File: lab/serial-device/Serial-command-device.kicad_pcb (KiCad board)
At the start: 2 copper layers, 78 x 64 mm, 4 parts, among them U1 atmega168p

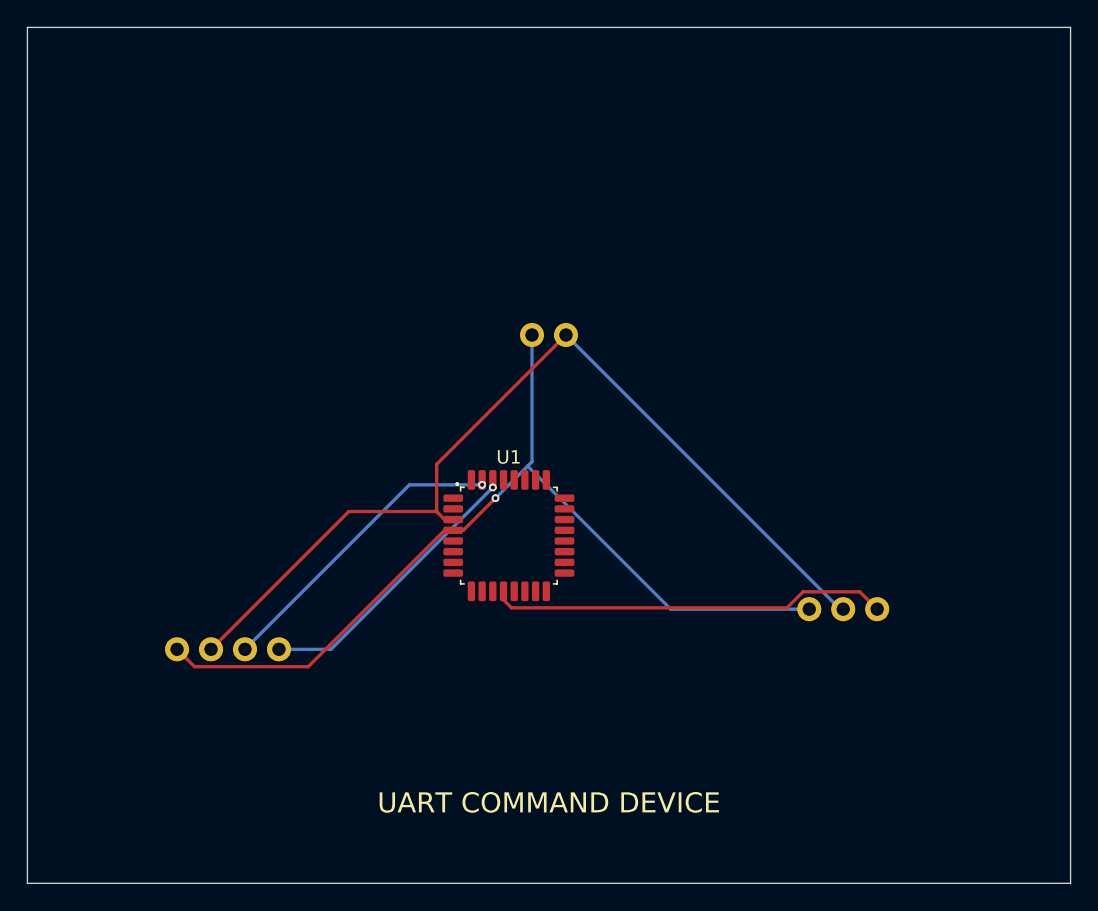
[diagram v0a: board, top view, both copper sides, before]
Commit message: lab: every board is a real board: an Arduino Nano and registry parts, routed, ready to order
The lab boards ran on simulation-only envelopes (labMcu, labDisplay, a battery). Now each is
an Arduino Nano on two sockets on the back (flashed over its USB, the image the app builds),
its lights LEDs through 1 kΩ, its knobs PTV09A pots, its display the MAX7219 eight-digit
module, its sensors an SHT31 and an SCD40 with their datasheets' support circuits, the FTDI
header for the serial console; the servo boards take 5 V on a screw terminal with a bulk
capacitor. All ten check complete with no errors or warnings, their firmware unchanged
(serial-device now on the 328P), and run in the lab without a fault (3 s each, dev host).

The registry: every interactive board must be ready to order and flash (publish.mjs refuses
one that is not; status simulation-only removed).

Claude-Session: https://claude.ai/code/session_01ATmMmxyrWxFwR3nTdXUrcx
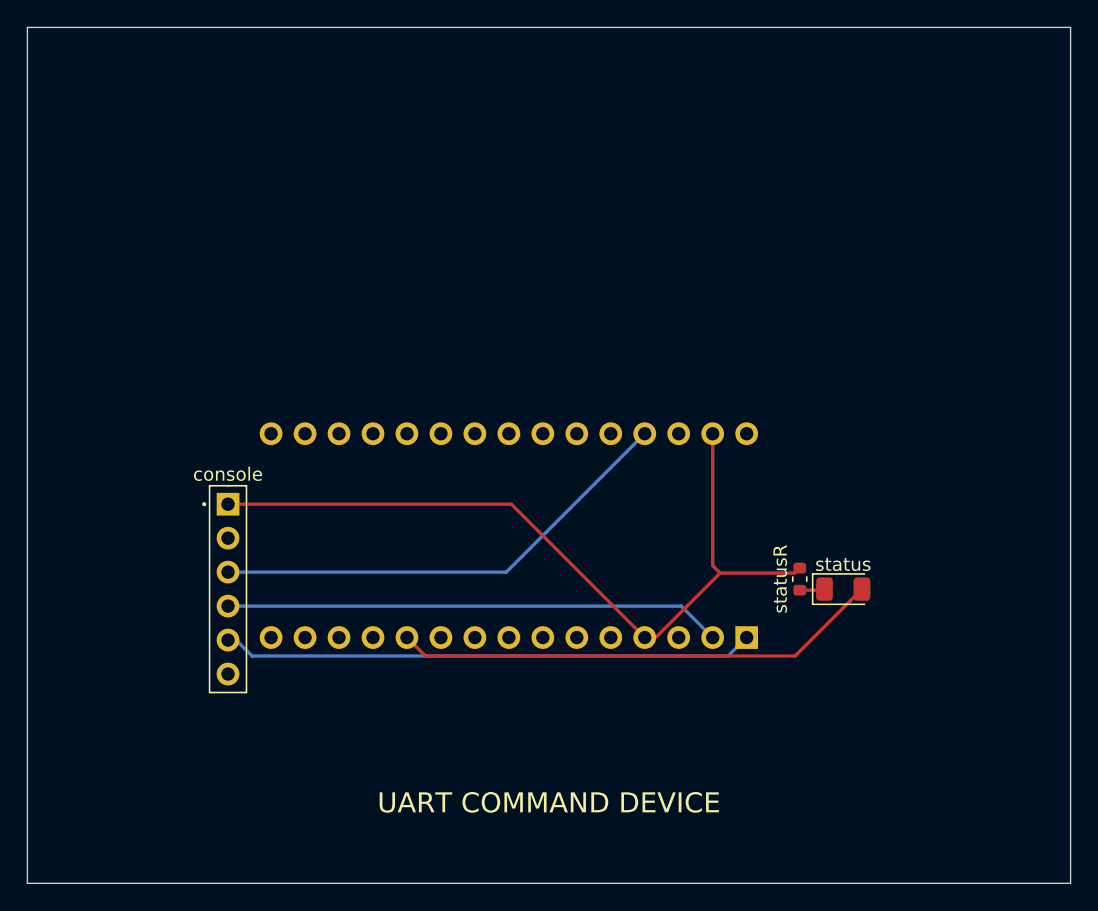
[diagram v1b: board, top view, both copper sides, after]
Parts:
- removed battery: battery, Regulated battery module
- removed the console at (115.0, 178.0)
- removed the status at (161.0, 178.0)
- added console: , PinHeader_1x06_P2.54mm_Vertical, F.Cu at (115.0, 178.0)
- added status: green, LED_1206_3216Metric, F.Cu at (161.0, 178.0)
- added statusR: 1kohm, R_0603_1608Metric, F.Cu at (157.8, 177.2)
- U1: value atmega168p -> A000005; footprint TQFP-32_7x7mm_P0.8mm -> Arduino_Nano_Socket_2x15_P2.54mm_W15.24mm; moved to B.Cu
- turned U1 to 90 degrees
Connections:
- U1 pad 1: (no net) -> TX
- U1 pad 11: (no net) -> LIGHT
- U1 pad 12: LIGHT -> (no net)
- U1 pad 2: (no net) -> RX
- U1 pad 27: (no net) -> V5
- U1 pad 29: (no net) -> GND
- U1 pad 3: GND -> (no net)
- U1 pad 30: RX -> (no net)
- U1 pad 4: V5 -> GND
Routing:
- net V5: track 68.4 -> 35.4 mm, vias 1 -> 0
- net TX: track 22.8 -> 39.8 mm, vias 1 -> 0
- net RX: track 21.0 -> 37.2 mm, vias 1 -> 0
- net GND: track 69.0 -> 58.3 mm
- net LIGHT: track 29.9 -> 36.7 mm
- net LIGHT_K: track 0.00 -> 2.09 mm

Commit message: Boards pass check and KiCad 10's DRC again: holes in courtyards, the USB net rename
pcbkit's check now has KiCad 10's pth/npth_inside_courtyard (pcbkit be5b6955), and 13 boards
failed it. KiCad's own DRC (kicad-cli 10) reports the same holes on every one of them.

- Parts that really stand above the holes under them (a screen or a Nano on its sockets, the
  Delta-S02's КМ-6 capacitors flat under its chips, as the factory placed them): a courtyard rule
  for the pair, written to each board's .kicad_dru, so KiCad's DRC agrees.
- Real collisions moved: servo-controller's dial 3 mm up (the Nano's socket pins came out under
  it), c3-pocket's fourth M3 hole from under a cell holder to the top edge's middle, s3-rgb's
  D-pad 2 mm up (a holder's peg came through under the down key).
- v003-emu, c3-pocket, rp2040-tft, rp2350-psram, s3-rgb, teensy41: re-routed for the standard USB
  block's renamed net (usb/raw is usb/vbusIn since pcbkit 2088839e): their tracks still carried
  the old name and shorted the fuse and connector pads.
- p4-touch-7: its board file still had a courtyard for the panel the design gives none (KiCad
  reported 114 courtyard errors); written again.

Measured on the dev host: all 44 registry boards `pcbkit check` complete with 0 errors, and
kicad-cli pcb drc 0 errors on every board.

Claude-Session: https://claude.ai/code/session_018URVYF1YPgyrMNetY9yT1T
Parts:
- console: value (none) -> PinHeader_1x06_P2.54mm_Vertical
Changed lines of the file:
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@@
   (footprint "Arduino_Nano_Socket_2x15_P2.54mm_W15.24mm" (layer "B.Cu") (at 136 174 90)
     (descr "Arduino Nano on two 1x15 female headers 15.24 mm apart, its USB end at +Y (Arduino's drawing): pins 1-15 the right row from the bottom (D1/TX … D12), 16-30 the left row from the top (D13 … VIN)")
+    (tags "THT module pin socket female header")
     (property "Reference" "U1" (at 0 -24.05 90) (layer "B.SilkS") (effects (font (size 1 1) (thickness 0.15)) (justify mirror)))
     (property "Value" "A000005" (at 0 0 0) (layer "B.Fab") (hide yes) (effects (font (size 1 1))))
@@
     (property "Status" "checked" (at 0 0 0) (layer "B.Fab") (hide yes) (effects (font (size 1 1))))
     (property "pcbkit" "U1" (at 0 0 0) (layer "B.Fab") (hide yes) (effects (font (size 1 1))))
-    (duplicate_pad_numbers_are_jumpers no)
     (fp_rect (start 9.25 21.85) (end -9.25 -23.35) (stroke (width 0.05) (type solid)) (layer "B.CrtYd"))
     (fp_line (start 0 -23.21) (end 9.11 -23.21) (stroke (width 0.12) (type solid)) (layer "B.SilkS"))
@@
   (footprint "PinHeader_1x06_P2.54mm_Vertical" (layer "F.Cu") (at 115 178 0)
     (descr "Through-hole straight pin header, 1x6, 2.54 mm pitch")
+    (tags "THT pin header")
     (property "Reference" "console" (at 0 -8.57 0) (layer "F.SilkS") (effects (font (size 1 1) (thickness 0.15))))
-    (property "Value" "" (at 0 0 0) (layer "F.Fab") (hide yes) (effects (font (size 1 1))))
+    (property "Value" "PinHeader_1x06_P2.54mm_Vertical" (at 0 0 0) (layer "F.Fab") (hide yes) (effects (font (size 1 1))))
     (property "pcbkit" "console" (at 0 0 0) (layer "F.Fab") (hide yes) (effects (font (size 1 1))))
-    (duplicate_pad_numbers_are_jumpers no)
     (fp_rect (start -1.52 7.87) (end 1.52 -7.87) (stroke (width 0.05) (type solid)) (layer "F.CrtYd"))
     (fp_line (start 0 -7.73) (end -1.38 -7.73) (stroke (width 0.12) (type solid)) (layer "F.SilkS"))
@@
   (footprint "LED_1206_3216Metric" (layer "F.Cu") (at 161 178 0)
     (descr "Chip LED 1206 (3216 metric), IPC-7351B nominal density")
+    (tags "chip 1206 3216Metric")
     (property "Reference" "status" (at 0 -1.83 0) (layer "F.SilkS") (effects (font (size 1 1) (thickness 0.15))))
     (property "Value" "green" (at 0 0 0) (layer "F.Fab") (hide yes) (effects (font (size 1 1))))
     (property "pcbkit" "status" (at 0 0 0) (layer "F.Fab") (hide yes) (effects (font (size 1 1))))
-    (duplicate_pad_numbers_are_jumpers no)
     (fp_rect (start -2.28 1.13) (end 2.28 -1.13) (stroke (width 0.05) (type solid)) (layer "F.CrtYd"))
     (fp_line (start 1.6 -1.135) (end -2.285 -1.135) (stroke (width 0.12) (type solid)) (layer "F.SilkS"))
@@
   (footprint "R_0603_1608Metric" (layer "F.Cu") (at 157.75 177.25 90)
     (descr "Chip resistor 0603 (1608 metric), IPC-7351B nominal density")
+    (tags "chip 0603 1608Metric")
     (property "Reference" "statusR" (at 0 -1.43 90) (layer "F.SilkS") (effects (font (size 1 1) (thickness 0.15))))
     (property "Value" "1kohm" (at 0 0 0) (layer "F.Fab") (hide yes) (effects (font (size 1 1))))
     (property "pcbkit" "statusR" (at 0 0 0) (layer "F.Fab") (hide yes) (effects (font (size 1 1))))
-    (duplicate_pad_numbers_are_jumpers no)
     (fp_rect (start -1.48 0.73) (end 1.48 -0.73) (stroke (width 0.05) (type solid)) (layer "F.CrtYd"))
     (fp_line (start -0.165 0.5225) (end 0.165 0.5225) (stroke (width 0.12) (type solid)) (layer "F.SilkS"))
@@
   (gr_text "UART COMMAND DEVICE" (at 139 194 0) (layer "F.SilkS") (effects (font (size 1.5 1.5) (thickness 0.15))))
   (group "pcbkit" (members "22687fff-f8ed-7975-b4d7-b6be23a86f2c"))
-  (gr_line (start 100 200) (end 178 200) (stroke (width 0.1) (type solid)) (layer "Edge.Cuts"))
-  (gr_line (start 178 200) (end 178 136) (stroke (width 0.1) (type solid)) (layer "Edge.Cuts"))
-  (gr_line (start 178 136) (end 100 136) (stroke (width 0.1) (type solid)) (layer "Edge.Cuts"))
-  (gr_line (start 100 136) (end 100 200) (stroke (width 0.1) (type solid)) (layer "Edge.Cuts"))
-  (segment (start 159.6 178) (end 159.525 178.075) (width 0.25) (layer "F.Cu") (net 3))
-  (segment (start 159.525 178.075) (end 159.6 178) (width 0.25) (layer "F.Cu") (net 3))
   (segment (start 159.6 178) (end 159.525 178.075) (width 0.25) (layer "F.Cu") (net 3))
   (segment (start 159.525 178.075) (end 157.75 178.075) (width 0.25) (layer "F.Cu") (net 3))
@@
   (segment (start 116.8 183) (end 115.61 181.81) (width 0.25) (layer "B.Cu") (net 5))
   (segment (start 115.61 181.81) (end 115 181.81) (width 0.25) (layer "B.Cu") (net 5))
+  (gr_line (start 100 200) (end 178 200) (stroke (width 0.1) (type solid)) (layer "Edge.Cuts"))
+  (gr_line (start 178 200) (end 178 136) (stroke (width 0.1) (type solid)) (layer "Edge.Cuts"))
+  (gr_line (start 178 136) (end 100 136) (stroke (width 0.1) (type solid)) (layer "Edge.Cuts"))
+  (gr_line (start 100 136) (end 100 200) (stroke (width 0.1) (type solid)) (layer "Edge.Cuts"))
 )
